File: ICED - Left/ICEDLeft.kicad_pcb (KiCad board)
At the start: 2 copper layers, 175.4 x 145 mm, 164 parts, among them P1 FLASH_HDR, P2 USBC, P3 CONN_17, P4 USB3_AFEMALE, Q1 TC1264, U1 MK20DX256VLH7, U2 IS31FL3731C, X1 CRYSTAL

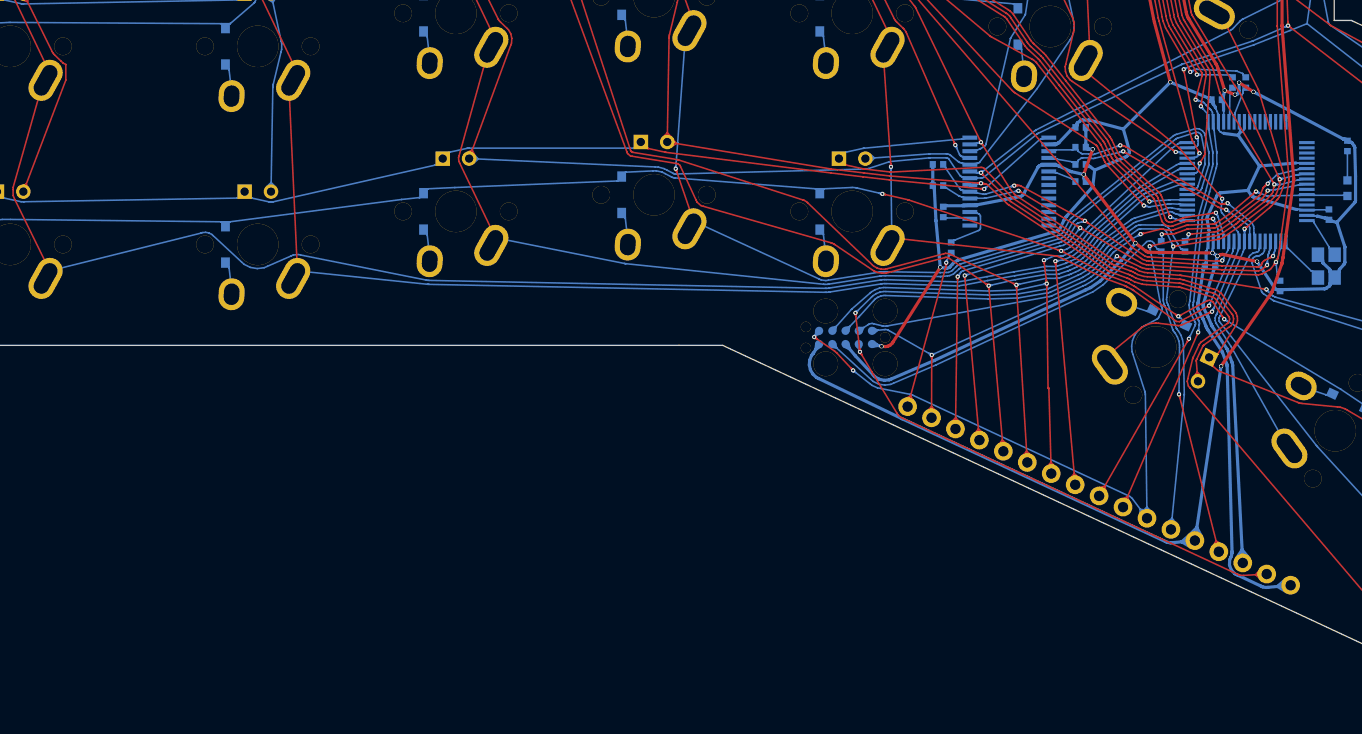
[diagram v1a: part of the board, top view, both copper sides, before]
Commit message: moved P1, P3, and S36
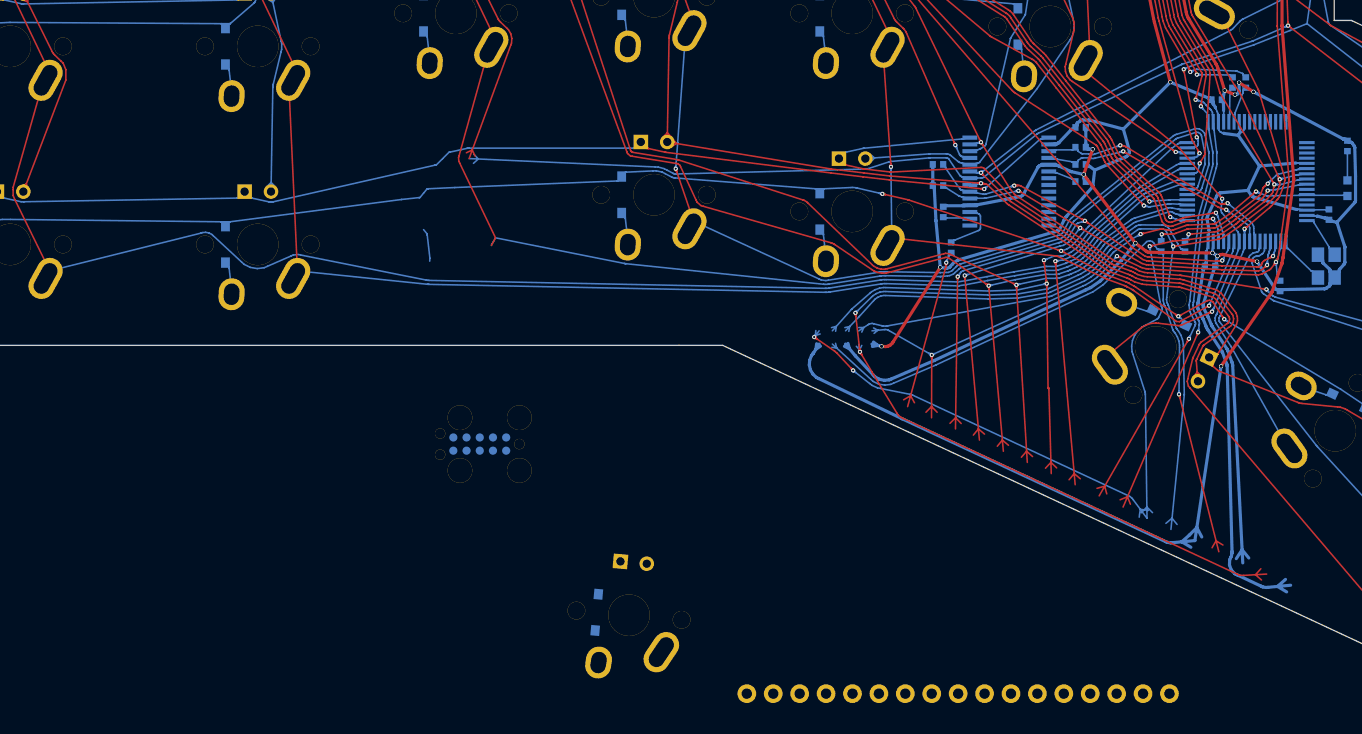
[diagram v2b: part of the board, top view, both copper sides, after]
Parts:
- moved D74 42.4 mm to (85.8, 156.4), turned to 355 degrees
- moved S36 42.2 mm to (85.4, 161.5), turned to 175 degrees
- moved D36 42.0 mm to (82.3, 161.2), turned to 175 degrees
- moved P1 36.6 mm to (71.0, 145.0)
- moved P3 23.4 mm to (117.0, 169.0), turned to 90 degrees
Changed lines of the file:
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@@
   )
   (module prettylib:JLINK_NEEDLE (layer Back)
-    (at 106.172 134.747 180)
+    (at 71 145 180)
     (tags jlink)
     (fp_text reference P1 (at -1.016 -4.572 180) (layer B.SilkS)
@@
   )
   (module prettylib:HEADER_1x17 (layer Back)
-    (at 130.556 149.987 65)
+    (at 117 169 90)
     (descr "Through-hole pin array, single row")
     (tags "HDR SIL")
-    (fp_text reference P3 (at -0.068247 23.293237 335) (layer B.SilkS)
+    (fp_text reference P3 (at -0.068247 23.293237 0) (layer B.SilkS)
       (effects (font (size 1 1) (thickness 0.2)) (justify mirror))
     )
@@
   )
   (module prettylib:INSW_LEDS_REG (layer Front)
-    (at 68.707 117.549)
+    (at 85.7938 156.39474 355)
     (attr smd)
-    (fp_text reference D74 (at 0 -1.5) (layer B.SilkS)
+    (fp_text reference D74 (at 0 -1.5 355) (layer B.SilkS)
       (effects (font (size 1 1) (thickness 0.2)) (justify mirror))
     )
-    (fp_text value LED (at 0 2.413) (layer F.SilkS) hide
+    (fp_text value LED (at 0 2.413 355) (layer F.SilkS) hide
       (effects (font (thickness 0.3048)))
     )
-    (pad 2 thru_hole oval (at 1.27 0) (size 1.4 1.4) (drill 0.8) (layers *.Cu *.Mask F.SilkS)
+    (pad 2 thru_hole oval (at 1.27 0 355) (size 1.4 1.4) (drill 0.8) (layers *.Cu *.Mask F.SilkS)
       (net 3 /ledmatrix/CA2))
-    (pad 1 thru_hole rect (at -1.27 0) (size 1.4 1.4) (drill 0.8) (layers *.Cu *.Mask F.SilkS)
+    (pad 1 thru_hole rect (at -1.27 0 355) (size 1.4 1.4) (drill 0.8) (layers *.Cu *.Mask F.SilkS)
       (net 10 /ledmatrix/CA9))
   )
@@
   )
   (module prettylib:SOT123-DIODE (layer Back)
-    (at 65.5955 122.629 180)
+    (at 82.25139 161.18423 175.0)
     (descr DIODE)
     (tags DIODE)
     (attr smd)
-    (fp_text reference D36 (at 0 3.81 450) (layer B.SilkS)
+    (fp_text reference D36 (at 0 3.81 445) (layer B.SilkS)
       (effects (font (size 1.016 1.016) (thickness 0.2032)) (justify mirror))
     )
-    (fp_text value DIODE (at 2.032 0 450) (layer B.SilkS) hide
+    (fp_text value DIODE (at 2.032 0 445) (layer B.SilkS) hide
       (effects (font (thickness 0.3048)) (justify mirror))
     )
@@
     (fp_line (start -0.8509 -1.45034) (end -0.8509 1.45034) (layer B.SilkS) (width 0.22098))
     (fp_line (start 0.8509 -1.45034) (end 0.8509 1.45034) (layer B.SilkS) (width 0.22098))
-    (pad 2 smd rect (at 0 1.7526 270) (size 1.00076 0.8509) (layers Back B.Paste B.Mask)
+    (pad 2 smd rect (at 0 1.7526 265) (size 1.00076 0.8509) (layers Back B.Paste B.Mask)
       (net 101 /Row5))
-    (pad 1 smd rect (at 0 -1.74752 270) (size 1.00076 0.8509) (layers Back B.Paste B.Mask)
+    (pad 1 smd rect (at 0 -1.74752 265) (size 1.00076 0.8509) (layers Back B.Paste B.Mask)
       (net 84 "Net-(D36-Pad1)"))
   )
@@
   )
   (module prettylib:MXALPS (layer Front)
-    (at 68.707 122.629 180)
+    (at 85.35105 161.4554 175)
     (descr MXALPS)
     (tags MXALPS)
-    (fp_text reference S36 (at 0 3.048 180) (layer B.SilkS)
+    (fp_text reference S36 (at 0 3.048 175) (layer B.SilkS)
       (effects (font (thickness 0.3048)) (justify mirror))
     )
-    (fp_text value SW (at -3.5 9 180) (layer B.SilkS) hide
+    (fp_text value SW (at -3.5 9 175) (layer B.SilkS) hide
       (effects (font (thickness 0.3048)) (justify mirror))
     )
@@
     (fp_line (start 7.62 7.62) (end -7.62 7.62) (layer Dwgs.User) (width 0.3))
     (fp_line (start -7.62 7.62) (end -7.62 -7.62) (layer Dwgs.User) (width 0.3))
-    (pad "" np_thru_hole circle (at 0 0 180) (size 3.98781 3.98781) (drill 3.9878) (layers *.Cu *.Mask F.SilkS)
+    (pad "" np_thru_hole circle (at 0 0 175) (size 3.98781 3.98781) (drill 3.9878) (layers *.Cu *.Mask F.SilkS)
       (clearance 0.1524))
-    (pad "" np_thru_hole circle (at -5.08 0 180) (size 1.70181 1.70181) (drill 1.7018) (layers *.Cu *.Mask F.SilkS)
+    (pad "" np_thru_hole circle (at -5.08 0 175) (size 1.70181 1.70181) (drill 1.7018) (layers *.Cu *.Mask F.SilkS)
       (clearance 0.1524))
-    (pad "" np_thru_hole circle (at 5.08 0 180) (size 1.70181 1.70181) (drill 1.7018) (layers *.Cu *.Mask F.SilkS)
+    (pad "" np_thru_hole circle (at 5.08 0 175) (size 1.70181 1.70181) (drill 1.7018) (layers *.Cu *.Mask F.SilkS)
       (clearance 0.1524))
-    (pad 1 thru_hole oval (at -3.405 -3.27 150.95) (size 2.5 4.17) (drill oval 1.5 3.17) (layers *.Cu *.Mask F.SilkS)
+    (pad 1 thru_hole oval (at -3.405 -3.27 145.95) (size 2.5 4.17) (drill oval 1.5 3.17) (layers *.Cu *.Mask F.SilkS)
       (net 117 /Col7))
-    (pad 2 thru_hole oval (at 2.52 -4.79 176.1) (size 2.5 3.08) (drill oval 1.5 2.08) (layers *.Cu *.Mask F.SilkS)
+    (pad 2 thru_hole oval (at 2.52 -4.79 171.1) (size 2.5 3.08) (drill oval 1.5 2.08) (layers *.Cu *.Mask F.SilkS)
       (net 84 "Net-(D36-Pad1)"))
   )
@@
   (segment (start 27.4 120) (end 26.6493 120.31777) (width 0.1524) (layer Front) (net 5))
   (segment (start 31.2 110) (end 27.115 120.724) (width 0.1524) (layer Front) (net 5))
-  (segment (start 31.2 110) (end 31.2 108.5) (width 0.1524) (layer Front) (net 5))
-  (segment (start 31.2 108.5) (end 30.9442 108.3764) (width 0.1524) (layer Front) (net 5))
+  (segment (start 31.2 110) (end 31.2 109) (width 0.1524) (layer Front) (net 5))
+  (segment (start 31.2 109) (end 30.9442 108.3764) (width 0.1524) (layer Front) (net 5))
   (segment (start 30.9442 108.3764) (end 30.733 108.1734) (width 0.1524) (layer Front) (net 5))
   (segment (start 30.1235 107.5868) (end 30.733 108.1734) (width 0.1524) (layer Front) (net 5))

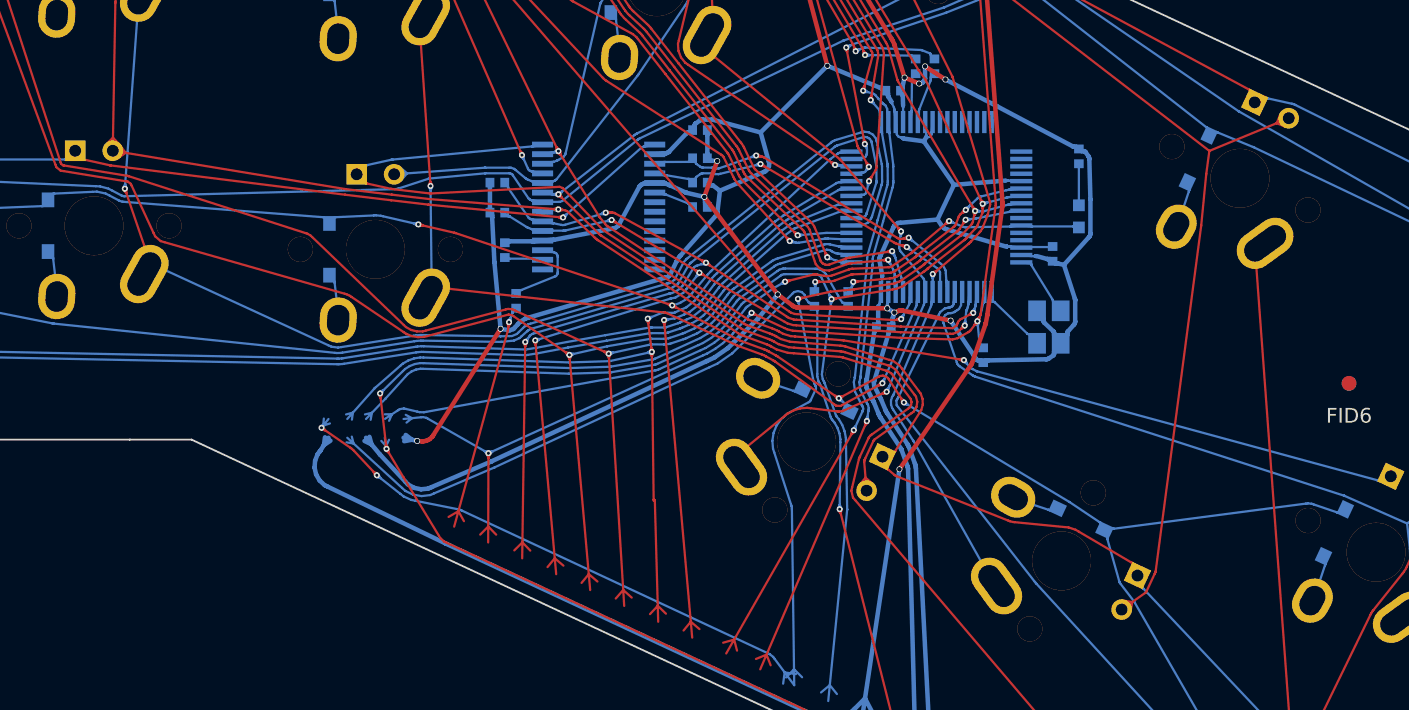
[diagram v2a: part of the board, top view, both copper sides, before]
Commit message: Moved S22 and the labesl for P3
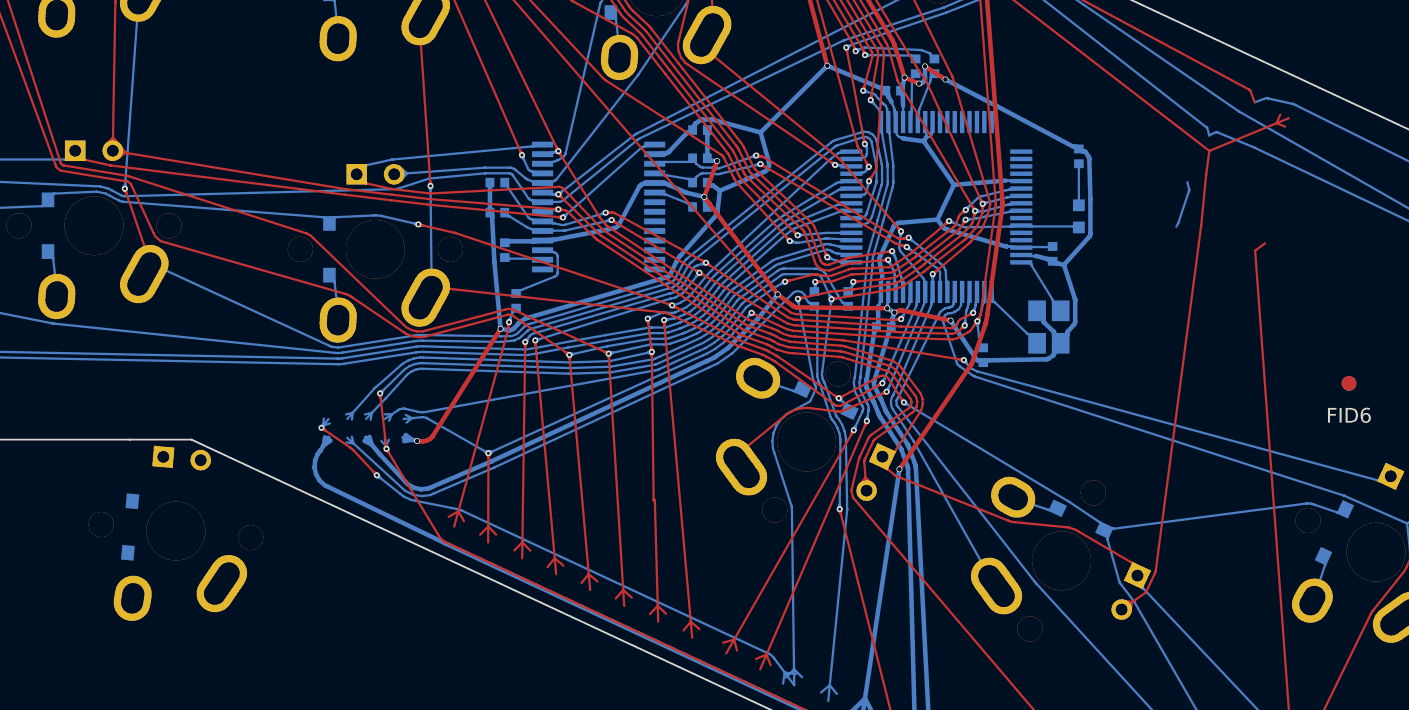
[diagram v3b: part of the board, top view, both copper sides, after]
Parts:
- moved D60 77.4 mm to (93.7, 136.8), turned to 355 degrees
- moved D22 76.5 mm to (90.2, 141.4), turned to 175 degrees
- moved S22 75.9 mm to (93.3, 141.7), turned to 175 degrees
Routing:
- net (no net): track 0.00 -> 45.0 mm
- net +5V: track 218.9 -> 213.7 mm
- net Net-(D36-Pad1): track 3.18 -> 0.00 mm
- net VDD: track 327.0 -> 323.9 mm
- net VSS: track 399.5 -> 396.5 mm
- net /mcu/TX0: track 177.4 -> 174.3 mm
- net /ledmatrix/CA2: track 431.6 -> 429.1 mm
- net /mcu/TX2: track 65.4 -> 62.9 mm
- net /mcu/SWD_CLK: track 70.8 -> 68.3 mm
- net /mcu/RX0: track 171.1 -> 168.6 mm
- net /mcu/MCU_RESET: track 102.1 -> 99.6 mm
- net /mcu/SCL0: track 72.1 -> 70.5 mm
- net /mcu/SDA0: track 70.7 -> 69.2 mm
- net /mcu/MOSI: track 172.4 -> 170.9 mm
- net /mcu/SWD_DIO: track 91.7 -> 90.2 mm
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
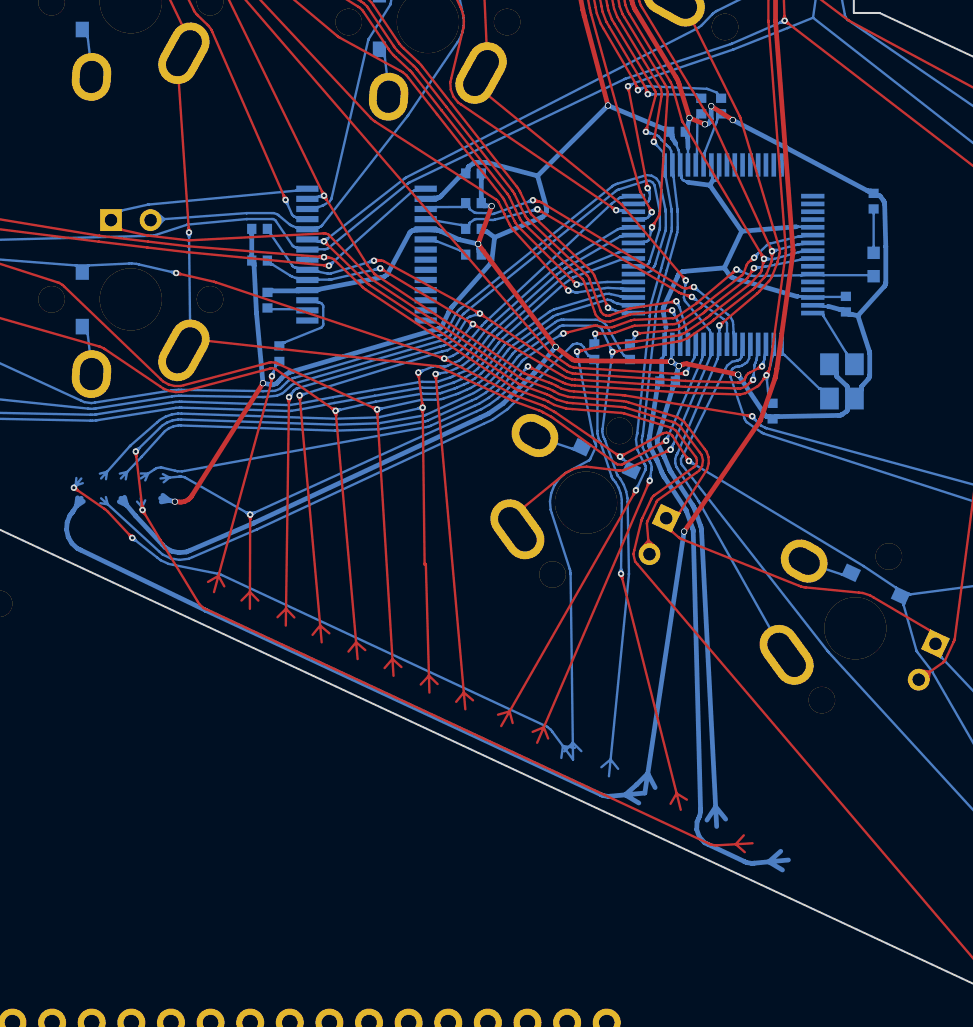
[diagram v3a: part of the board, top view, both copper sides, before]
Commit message: Moved U1, the MPU, and the entourage of resisters and capaciters.
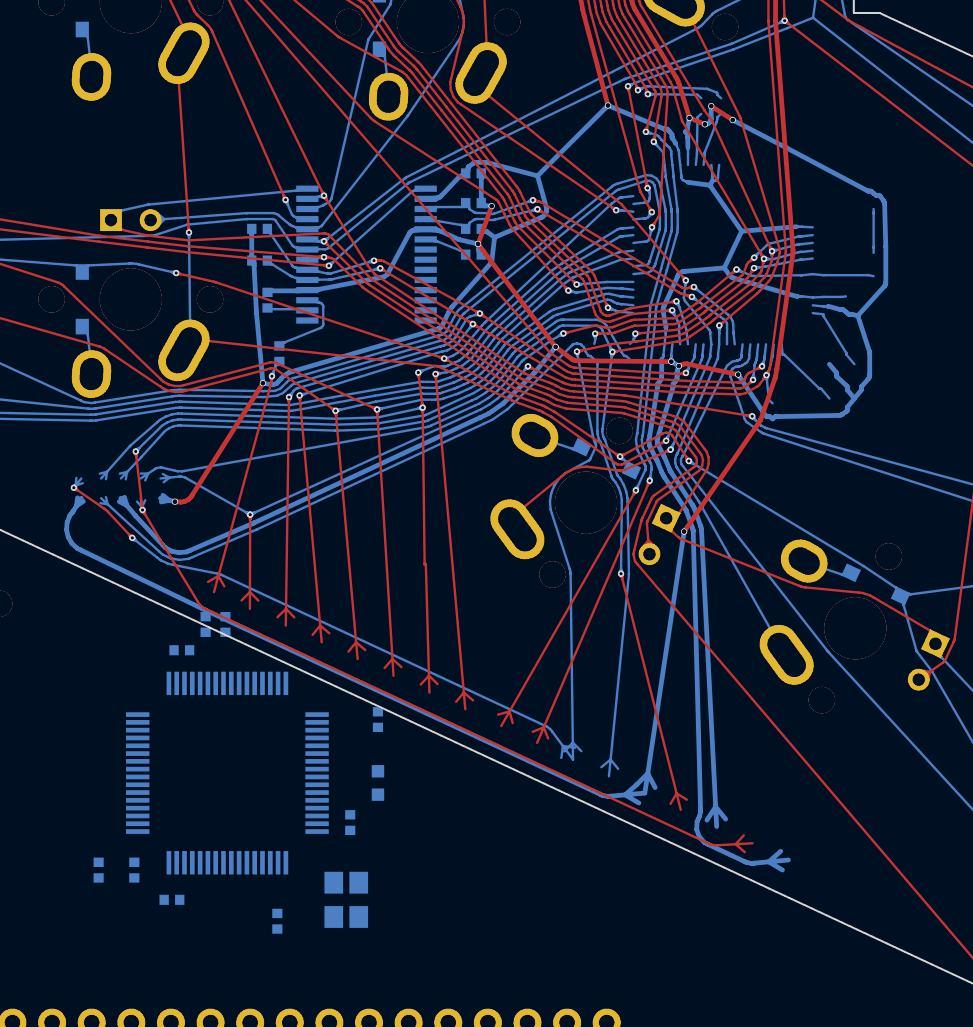
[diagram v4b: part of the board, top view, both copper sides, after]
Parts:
- moved C4 46.0 mm to (110.1, 145.1)
- moved R6 46.0 mm to (104.7, 159.2)
- moved R7 46.0 mm to (107.0, 159.2)
- moved C7 46.0 mm to (120.9, 156.2)
- moved R1 46.0 mm to (111.6, 143.5)
- moved U1 46.0 mm to (113.0, 153.0)
- moved R11 46.0 mm to (122.7, 149.6)
- moved X1 46.0 mm to (120.6, 161.1)
- moved C3 46.0 mm to (109.4, 161.1)
- moved D77 46.0 mm to (122.7, 153.6)
- moved R2 46.0 mm to (112.9, 143.5)
- moved C5 45.6 mm to (116.2, 162.5)
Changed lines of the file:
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@@
   )
   (module prettylib:LQFP64 (layer Back)
-    (at 144.78 119.761 270)
+    (at 113 153 270)
     (descr "Quad Flat Package w/ Pins")
     (tags "QFP TQFP LQFP")
@@
   )
   (module prettylib:SMD-1005 (layer Back)
-    (at 138.811 125.984 180)
+    (at 107.031 159.223 180)
     (attr smd)
     (fp_text reference R7 (at 0 1.524 180) (layer B.SilkS)
@@
   )
   (module prettylib:SMD-1005 (layer Back)
-    (at 154.432 116.332)
+    (at 122.652 149.571)
     (attr smd)
     (fp_text reference R11 (at 0 1.524) (layer B.SilkS)
@@
   )
   (module prettylib:SMD-1005 (layer Back)
-    (at 136.525 125.984 180)
+    (at 104.745 159.223 180)
     (attr smd)
     (fp_text reference R6 (at 0 1.524 180) (layer B.SilkS)
@@
   )
   (module prettylib:SMD-1005 (layer Back)
-    (at 147.955 129.794 180)
+    (at 116.2 162.5 180)
     (attr smd)
     (fp_text reference C5 (at 0 1.524 180) (layer B.SilkS)
@@
   )
   (module prettylib:SMD-1005 (layer Back)
-    (at 152.654 122.936 180)
+    (at 120.874 156.175 180)
     (attr smd)
     (fp_text reference C7 (at 0 1.524 180) (layer B.SilkS)
@@
   )
   (module prettylib:SMD-1005 (layer Back)
-    (at 141.224 127.889 270)
+    (at 109.444 161.128 270)
     (attr smd)
     (fp_text reference C3 (at 0 1.524 270) (layer B.SilkS)
@@
   )
   (module prettylib:SMD-1005 (layer Back)
-    (at 144.653 110.236 180)
+    (at 112.873 143.475 180)
     (attr smd)
     (fp_text reference R2 (at 0 1.524 180) (layer B.SilkS)
@@
   )
   (module prettylib:SMD-1005 (layer Back)
-    (at 141.859 111.887 270)
+    (at 110.079 145.126 270)
     (attr smd)
     (fp_text reference C4 (at 0 1.524 270) (layer B.SilkS)
@@
   )
   (module prettylib:SMD-1005 (layer Back)
-    (at 143.383 110.236 180)
+    (at 111.603 143.475 180)
     (attr smd)
     (fp_text reference R1 (at 0 1.524 180) (layer B.SilkS)
@@
   )
   (module prettylib:LED-0603 (layer Back)
-    (at 154.432 120.396 90)
+    (at 122.652 153.635 90)
     (descr "LED 0603 smd package")
     (tags "LED led 0603 SMD smd SMT smt smdled SMDLED smtled SMTLED")
@@
   )
   (module prettylib:NX3225SA (layer Back)
-    (at 152.4 127.889 270)
+    (at 120.62 161.128 270)
     (descr NX3225SA)
     (tags NX3225SA)
